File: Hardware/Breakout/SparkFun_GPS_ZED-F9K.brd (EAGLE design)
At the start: 43.2 x 43.2 mm, 104 parts, among them J1 QWIIC_RIGHT_ANGLE, J4 U.FL, J6 QWIIC_RIGHT_ANGLE, U2 3.3V, U3 UBLOX_ZED_F9K, U4 TRIPLE_BUFFER_74LVC3G07

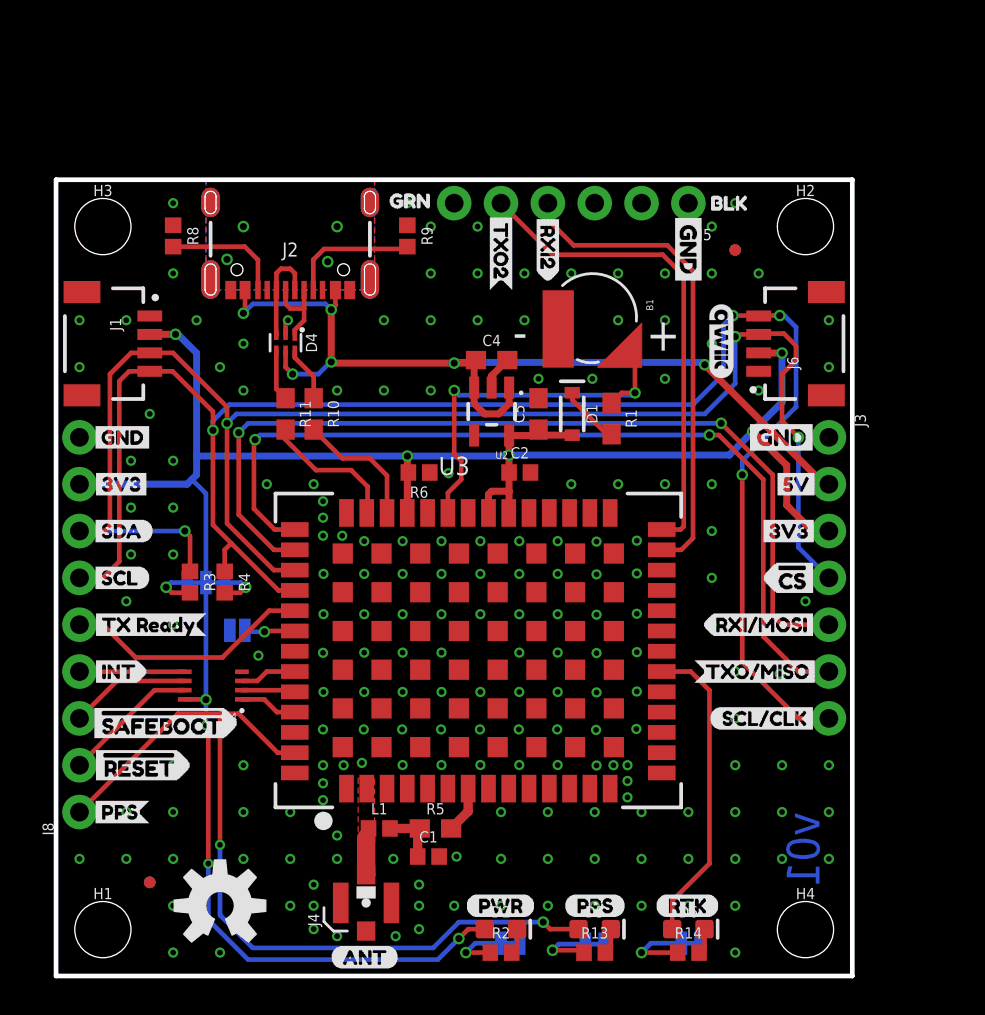
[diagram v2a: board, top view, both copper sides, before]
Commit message: Updates breakout board with the same parts as the pi hat
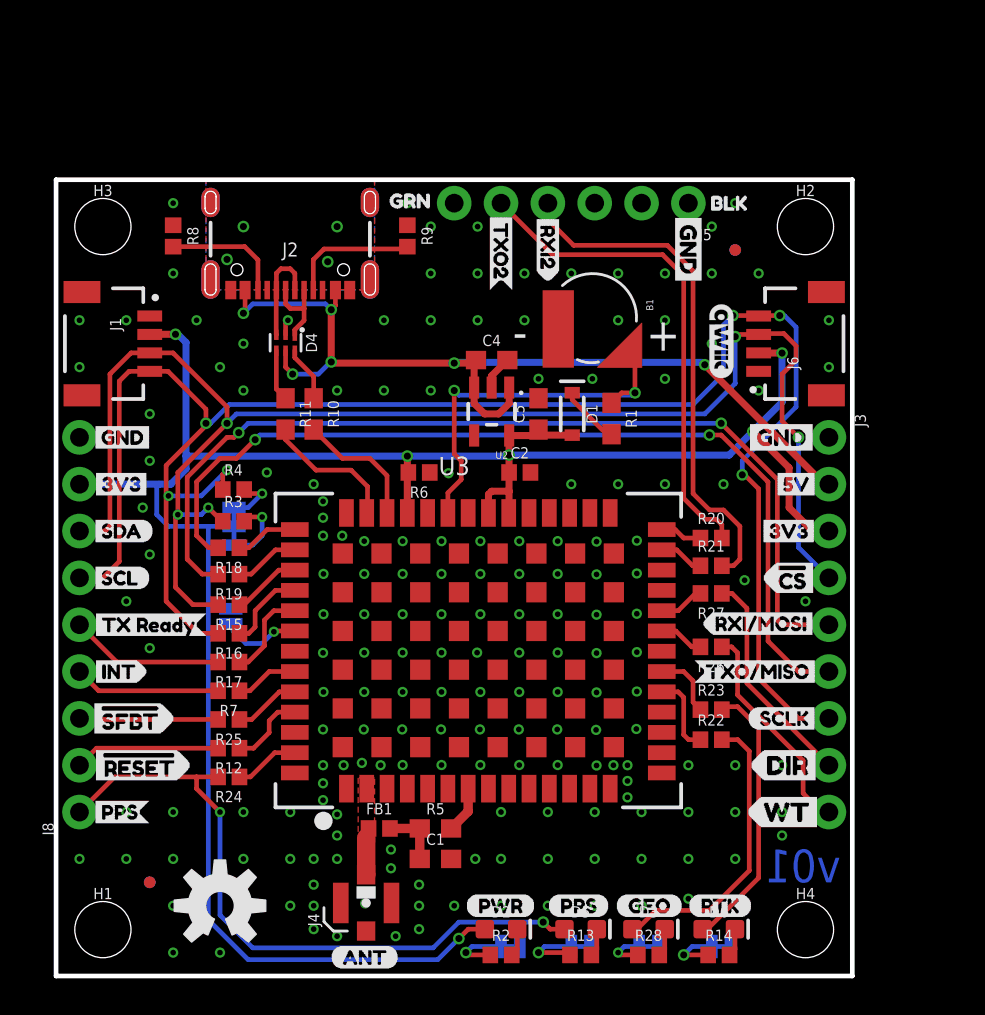
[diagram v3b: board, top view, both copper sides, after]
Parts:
- removed U4: TRIPLE_BUFFER_74LVC3G07, classified:SOP_8-PIN
- added D3: BLUE, SparkFun-LED:LED-0603
- added GEO: JUMPER-SMT_2_NC_TRACE_SILK, SparkFun-Jumpers:SMT-JUMPER_2_NC_TRACE_SILK
- added R12, R15, R16, R17, R18, R19, R20, R21, R22, R23, R24, R25, R26, R27, R7: 33, SparkFun-Resistors:0402
- added R28: 1KOHM-0402-1/16W-1%, SparkFun-Resistors:0402
- added U$32: (no value), wt_dir:DIR3
- added U$55: (no value), wat-for-reals:#SFBT0
- added U$56, U$58: (no value), wat-for-reals:GEO1
- added U$57: (no value), wat-for-reals:SCLK2
- C1: value 0.1uF -> 47pF; device SparkFun-Capacitors:0402 -> SparkFun-Capacitors:0603
- FB1: value 3.9NH -> FERRITE_BEAD-120_OHM-0402
- J3: device SparkFun-Connectors:1X07_NO_SILK -> SparkFun-Connectors:1X09_NO_SILK
- R5: value 20 -> 10
- U$10: device corrected_safe_reset:#SAFEBOOT0 -> wt_dir:DIR1
- U$13: device ALL labels:SCL#CLK7 -> wt_dir:WT0
- U$50: device NEO_GPS_board_silk_FINAL#03#jpg:NEO_GPS_BOARD_SILK_FINAL#03#JPG -> wt_dir:WT2
- U3: value UBLOX_ZED_F9K -> UBLOX_ZED_F9R; device classified:UBLOX_ZED_F9K -> classified:UBLOX_ZED_F9R
- moved U$10 40.3 mm to (41.7, 11.4), flipped to the bottom
- moved U$50 16.1 mm to (37.5, 8.89), flipped to the top
- moved U$13 8.03 mm to (41.7, 8.89), flipped to the bottom
- moved R4 5.04 mm to (9.62, 26.4), turned to 0 degrees
- moved R3 4.06 mm to (9.62, 24.7), turned to 0 degrees
- moved JP2 3.41 mm to (9.65, 24.4), turned to 90 degrees
- moved U$8 1.78 mm to (34.3, 3.81)
- moved U$46 1.76 mm to (11.6, 22.5), turned to 90 degrees
- moved RTK 1.66 mm to (36.1, 1.60)
- moved R14 1.66 mm to (35.9, 1.14)
- moved U$22 1.66 mm to (37.7, 3.43)
- moved D6 1.65 mm to (35.9, 2.54)
- moved U$4 0.89 mm to (26.7, 3.81)
- moved JP1 0.84 mm to (9.47, 19.5), turned to 90 degrees
- moved U$47 0.77 mm to (30.1, 3.43)
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- renumbered L1 to FB1
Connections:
- removed net !RESET_IN: U3.P49, U4.P3
- removed net !RESET_OUT: J8.2, U4.P7
- removed net !SAFEBOOT_IN: J8.3, U4.P6
- removed net !SAFEBOOT_OUT: U3.P50, U4.P2
- removed net INT_IN: U3.P51, U4.P1
- removed net INT_OUT: J8.4, U4.P5
- new net !RESET: J8.4, R7.2
- new net !SAFEBOOT: J8.3, R25.2
- new net DIR: J3.8, R27.1
- new net GEOF_STAT: D3.A, R22.2
- new net INT: J8.2, R12.2
- new net N$11: R7.1, U3.P49
- new net N$12: R12.1, U3.P51
- new net N$16: R15.1, U3.P44
- new net N$17: R16.1, U3.P45
- new net N$18: R17.1, U3.P46
- new net N$19: R18.1, U3.P42
- new net N$20: R19.1, U3.P43
- new net N$21: R20.1, U3.P27
- new net N$26: R21.1, U3.P26
- new net N$27: R22.1, U3.P19
- new net N$28: R23.1, U3.P20
- new net N$29: R24.1, U3.P53
- new net N$30: R25.1, U3.P50
- new net N$31: R26.2, U3.P22
- new net N$32: R27.2, U3.P23
- new net N$33: GEO.2, R28.1
- new net N$34: D3.C, R28.2
- new net WT: J3.9, R26.1
- net 3.3V: no longer U4.P8
- net GND: now also GEO.1; no longer U4.P4
- net PPS: now also R24.2; no longer U3.P53
- net RTK_STAT: now also R23.2; no longer U3.P20
- net RXI/MOSI: now also R19.2; no longer U3.P43
- net RXI2: now also R21.2; no longer U3.P26
- net SCL/CLK: now also R16.2; no longer U3.P45
- net SDA/!CS: now also R15.2; no longer U3.P44
- net TXO/MISO: now also R18.2; no longer U3.P42
- net TXO2: now also R20.2; no longer U3.P27
- net TX_READY: now also R17.2; no longer U3.P46
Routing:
- net GEOF_STAT: track 0.00 -> 15.9 mm
- net DIR: track 0.00 -> 12.0 mm
- net WT: track 0.00 -> 11.9 mm
- net PPS: track 46.6 -> 36.5 mm
- net !RESET: track 0.00 -> 7.95 mm
- net INT: track 0.00 -> 7.90 mm
- net !SAFEBOOT: track 0.00 -> 7.54 mm
- net !RESET_OUT: track 7.40 -> 0.00 mm
- net !SAFEBOOT_IN: track 6.55 -> 0.00 mm
- net INT_OUT: track 5.71 -> 0.00 mm
- net SCL/CLK: track 93.9 -> 99.6 mm, vias 4 -> 6
- net TX_READY: track 13.5 -> 8.36 mm
- net N$18: track 0.00 -> 4.97 mm
- net N$17: track 0.00 -> 4.49 mm
- net N$27: track 0.00 -> 4.36 mm
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
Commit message: Touches up some vias and traces
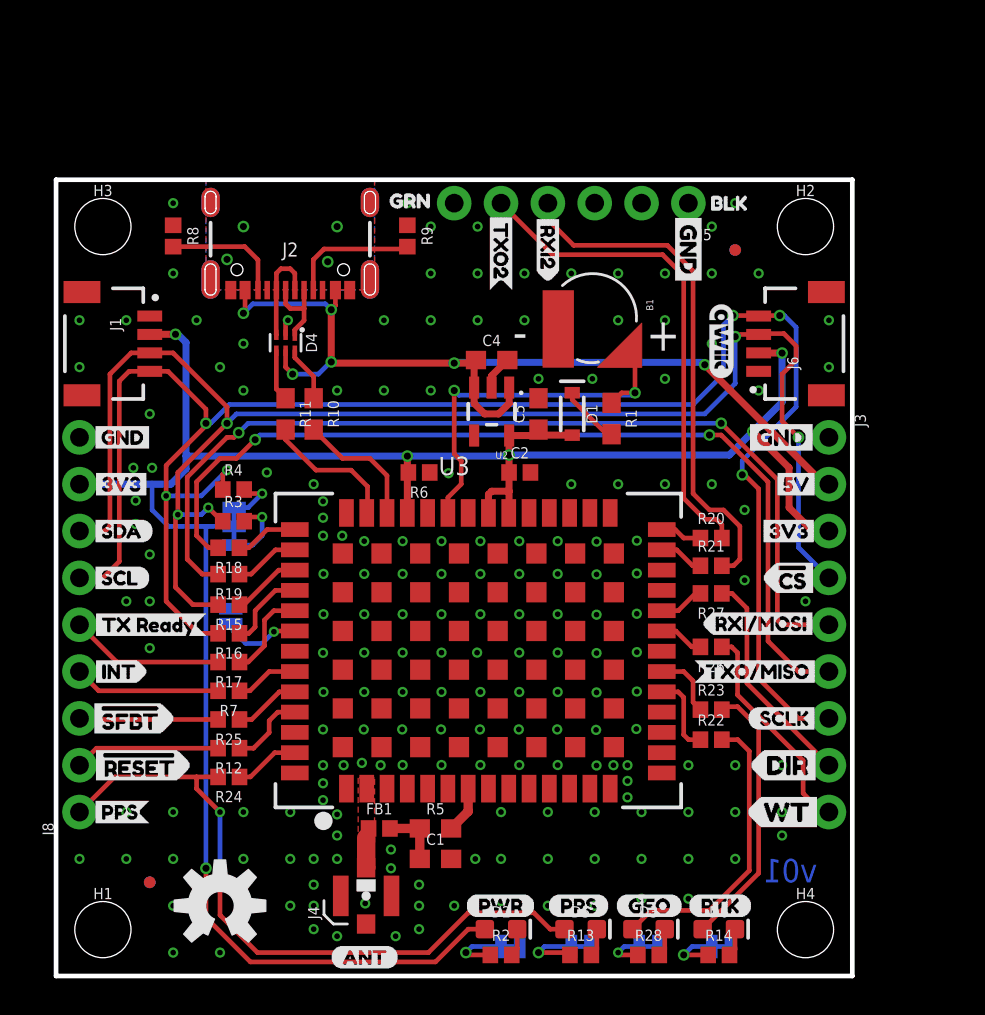
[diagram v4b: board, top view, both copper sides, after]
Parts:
- moved J4 0.38 mm to (16.8, 4.34)
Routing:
- net PPS: track 36.5 -> 37.1 mm
- net GND: vias 180 -> 184

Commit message: Gerbers for both boards
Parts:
- removed C5: 1.0uF, SparkFun-Capacitors:0603
- removed H3: STAND-OFFTIGHT, SparkFun-Hardware:STAND-OFF-TIGHT
- removed J8: (no value), SparkFun-Connectors:1X09_NO_SILK
- removed PPS, PWR: JUMPER-SMT_2_NC_TRACE_SILK, SparkFun-Jumpers:SMT-JUMPER_2_NC_TRACE_SILK
- added $1_36_$_2020-02-13_17-32-45: STAND-OFFTIGHT, SparkFun-Hardware:STAND-OFF-TIGHT
- added C3: 1.0uF, SparkFun-Capacitors:0603
- added J7: (no value), SparkFun-Connectors:1X06_NO_SILK
- added JP5: JUMPER-SMT_2_NO_SILK, SparkFun-Jumpers:SMT-JUMPER_2_NO_SILK
- added JP6: JUMPER-SMT_3_2-NC_TRACE_SILK, SparkFun-Jumpers:SMT-JUMPER_3_2-NC_TRACE_SILK
- C1: value 47pF -> 1.0uF; device SparkFun-Capacitors:0603 -> SparkFun-Capacitors:0402
- C2: value 1.0uF -> 47pF; device SparkFun-Capacitors:0402 -> SparkFun-Capacitors:0603
- D1: value 0.5A/40V/420mV -> RED; device SparkFun-DiscreteSemi:SOD-323 -> SparkFun-LED:LED-0603
- D2: value RED -> BLUE
- D4: value PRTR5V0U2F -> BLUE; device SparkFun-IC-Power:SOT886 -> SparkFun-LED:LED-0603
- D5: value BLUE -> PRTR5V0U2F; device SparkFun-LED:LED-0603 -> SparkFun-IC-Power:SOT886
- D6: value BLUE -> 0.5A/40V/420mV; device SparkFun-LED:LED-0603 -> SparkFun-DiscreteSemi:SOD-323
- J1: value QWIIC_RIGHT_ANGLE -> U.FL; device SparkFun-Connectors:JST04_1MM_RA -> SparkFun-Connectors:U.FL
- J3: value (none) -> QWIIC_RIGHT_ANGLE; device SparkFun-Connectors:1X09_NO_SILK -> SparkFun-Connectors:JST04_1MM_RA
- J4: value U.FL -> QWIIC_RIGHT_ANGLE; device SparkFun-Connectors:U.FL -> SparkFun-Connectors:JST04_1MM_RA
- J5: device SparkFun-Connectors:1X06_NO_SILK -> SparkFun-Connectors:1X09_NO_SILK
- J6: value QWIIC_RIGHT_ANGLE -> (none); device SparkFun-Connectors:JST04_1MM_RA -> SparkFun-Connectors:1X09_NO_SILK
- JP1: value JUMPER-SMT_2_NO_SILK -> JUMPER-SMT_2_NC_TRACE_SILK; device SparkFun-Jumpers:SMT-JUMPER_2_NO_SILK -> SparkFun-Jumpers:SMT-JUMPER_2_NC_TRACE_SILK
- JP2: value JUMPER-SMT_3_2-NC_TRACE_SILK -> JUMPER-SMT_2_NC_TRACE_SILK; device SparkFun-Jumpers:SMT-JUMPER_3_2-NC_TRACE_SILK -> SparkFun-Jumpers:SMT-JUMPER_2_NC_TRACE_SILK
- LOGO1: value SFE_LOGO_NAME_FLAME.2_INCH -> OSHW-LOGOM; device SparkFun-Aesthetics:SFE_LOGO_NAME_FLAME_.2 -> SparkFun-Aesthetics:OSHW-LOGO-M
- LOGO3: value OSHW-LOGOM -> SFE_LOGO_NAME_FLAME.2_INCH; device SparkFun-Aesthetics:OSHW-LOGO-M -> SparkFun-Aesthetics:SFE_LOGO_NAME_FLAME_.2
- R1: value 3.3k -> 100K; device SparkFun-Resistors:0603 -> SparkFun-Resistors:0402
- R10, R11: value 27 -> 33; device SparkFun-Resistors:0603 -> SparkFun-Resistors:0402
- R13, R14, R2: value 1KOHM-0402-1/16W-1% -> 33
- R17: value 33 -> 10; device SparkFun-Resistors:0402 -> SparkFun-Resistors:0603
- R18, R20: value 33 -> 5.1k
- R19, R25: value 33 -> 2.2K
- R21, R22, R23, R24: value 33 -> 1KOHM-0402-1/16W-1%
- R26, R27: value 33 -> 27; device SparkFun-Resistors:0402 -> SparkFun-Resistors:0603
- R28: value 1KOHM-0402-1/16W-1% -> 3.3k; device SparkFun-Resistors:0402 -> SparkFun-Resistors:0603
- R3, R4: value 2.2K -> 33
- R5: value 10 -> 33; device SparkFun-Resistors:0603 -> SparkFun-Resistors:0402
- R6: value 100K -> 33
- R8, R9: value 5.1k -> 33
- moved FD1 46.7 mm to (5.08, 5.08)
- moved FD4 46.7 mm to (36.8, 39.4), flipped to the bottom
- moved J6 44.7 mm to (1.27, 8.89)
- moved H2 38.1 mm to (2.54, 40.6)
- moved D4 37.4 mm to (32.1, 2.54), turned to 0 degrees
- moved J3 37.2 mm to (5.08, 34.3)
- moved J4 36.7 mm to (38.1, 34.3)
- moved D5 35.6 mm to (12.4, 34.3), turned to 270 degrees
- moved J1 32.2 mm to (16.8, 4.34), turned to 90 degrees
- moved JP2 29.5 mm to (28.4, 1.60), turned to 0 degrees
- moved R28 29.2 mm to (30.1, 30.2), turned to 270 degrees
- moved D6 29.0 mm to (28.0, 30.5), turned to 270 degrees
- moved LOGO1 28.4 mm to (8.89, 3.81), flipped to the top
- moved LOGO3 28.4 mm to (21.6, 29.2), flipped to the bottom
- moved D1 28.2 mm to (24.1, 2.54), turned to 0 degrees
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- renumbered B1 to BT1, FRAME2 to FRAME1, GEO to JP4, RTK to JP3, U3 to U1
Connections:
- net !RESET: now also J6.4, R4.2; no longer J8.4, R7.2
- net !SAFEBOOT: now also J6.3, R16.2; no longer J8.3, R25.2
- net 3.3V: now also C1.1, C4.1, D6.A, J3.2, J4.2, J5.3, J6.8, JP6.2, R1.2; no longer C2.1, C5.1, D2.A, J1.2, J3.3, J6.2, J8.8, JP2.2, R6.2
- net DIR: now also J5.8, R3.1; no longer J3.8, R27.1
- net DMINUS: now also R26.2; no longer R10.2
- net DPLUS: now also R27.2; no longer R11.2
- net D_SEL: now also JP5.1; no longer JP1.1
- net GEOF_STAT: now also D4.A, R13.2; no longer D3.A, R22.2
- net GND: now also C3.2, D5.2, J1.2, J6.9, J7.1, JP1.1, JP2.1, JP5.2, R1.1, R18.1, R20.1; no longer C5.2, D4.2, J4.2, J6.1, J8.9, JP1.2, PPS.1, PWR.1, R6.1, R8.1, R9.1
- net INT: now also J6.2, R5.2; no longer J8.2, R12.2
- net N$1: now also JP6.1, R25.2; no longer JP2.1, R3.2
- net N$10: now also D5.4, R27.1; no longer D4.4, R11.1
- net N$11: now also R4.1; no longer R7.1
- net N$12: now also R5.1; no longer R12.1
- net N$14: now also R18.2; no longer R8.2
- net N$15: now also R20.2; no longer R9.2
- net N$16: now also R6.1; no longer R15.1
- net N$17: now also R7.1; no longer R16.1
- net N$18: now also R8.1; no longer R17.1
- net N$19: now also R9.1; no longer R18.1
- net N$2: now also D6.C, R28.2; no longer D1.C, R1.2
- net N$20: now also R10.1; no longer R19.1
- net N$21: now also R11.1; no longer R20.1
- net N$22: now also R23.1; no longer R14.1
- net N$23: now also JP2.2, R22.1; no longer PPS.2, R13.1
- net N$24: now also D2.C, R22.2; no longer D5.C, R13.2
- net N$25: now also D3.C, R23.2; no longer D6.C, R14.2
- net N$26: now also R12.1; no longer R21.1
- net N$27: now also R13.1; no longer R22.1
- net N$28: now also R14.1; no longer R23.1
- net N$29: now also R15.1; no longer R24.1
- net N$3: now also JP6.3, R19.2; no longer JP2.3, R4.2
- net N$30: now also R16.1; no longer R25.1
- net N$31: now also R2.2; no longer R26.2
- net N$32: now also R3.2; no longer R27.2
- net N$33: now also R24.1; no longer R28.1
- net N$34: now also D4.C, R24.2; no longer D3.C, R28.2
- net N$4: now also D1.C, R21.2; no longer D2.C, R2.2
- net N$5: now also C2.1, R17.1; no longer C1.1, R5.1
- net N$6: now also D5.3; no longer D4.3
- net N$7: now also D5.1; no longer D4.1
- net N$8: now also JP1.2, R21.1; no longer PWR.2, R2.1
- net N$9: now also D5.6, R26.1; no longer D4.6, R10.1
- net PPS: now also D2.A, J6.1, R15.2; no longer D5.A, J8.1, R24.2
- net RF_IN: now also J1.FEED; no longer J4.FEED
- net RTK_STAT: now also D3.A, R14.2; no longer D6.A, R23.2
- net RXI/MOSI: now also J5.5, R10.2; no longer J3.5, R19.2
- net RXI2: now also J7.4, R12.2; no longer J5.4, R21.2
- net SCL/CLK: now also J3.4, J4.4, J5.7, J6.6, R19.1, R7.2; no longer J1.4, J3.7, J6.4, J8.6, R16.2, R4.1
- net SDA/!CS: now also J3.3, J4.3, J5.4, J6.7, R25.1, R6.2; no longer J1.3, J3.4, J6.3, J8.7, R15.2, R3.1
- net TXO/MISO: now also J5.6, R9.2; no longer J3.6, R18.2
- net TXO2: now also J7.5, R11.2; no longer J5.5, R20.2
- net TX_READY: now also J6.5, R8.2; no longer J8.5, R17.2
- net VIN: now also C3.1, D5.5, J5.2; no longer C4.1, D4.5, J3.2
- net V_BATT: now also R28.1; no longer R1.1
- net V_RF: now also R17.2; no longer R5.2
- net WT: now also J5.9, R2.1; no longer J3.9, R26.1
